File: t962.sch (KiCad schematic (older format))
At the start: 40 parts, among them J1 Conn_01x03, J10 Conn_01x04, J2 TE 282834-8, J3 Conn_01x02_Male, J4 Conn_01x02_Male, J5 Conn_01x02_Male, J7 2.54mm pin header, J8 USB_B_Micro, Q1 BSS214NW, SW1 SW_SPST_KMR2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

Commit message: Added more part number information.
Signed-off-by: Aaron Williams <aaron.w2@gmail.com>
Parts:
- SW2: MFR (none) -> C&K; MPN (none) -> KMR231NG LFS; SPN (none) -> CKN10246CT-ND; SPR (none) -> Digikey; SPURL (none) -> https://www.digikey.com/product-detail/en/c-k/KMR231NG-LFS/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
- U1, U3, U4: MFR (none) -> Maxim; MPN (none) -> MAX31850KATB+; SPN (none) -> MAX31850KATB+-ND; SPR (none) -> Digikey; SPURL (none) -> https://www.digikey.com/product-detail/en/maxim-integrated/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
- U2: MFR (none) -> STMicroelectronics; SPN (none) -> 497-1241-1-ND; SPR (none) -> Digikey; SPURL (none) -> /product-detail/en/stmicroelectronics/LD1117S33CTR/497-1241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
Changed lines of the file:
@@
 F 1 "MAX31850KATB+" H 2250 1934 50  0000 C CNN
 F 2 "Aaron:TDFN-10_3x4mm_P0.5mm" H 2250 1500 50  0001 C CNN
-F 3 "" H 2250 1500 50  0001 C CNN
+F 3 "https://datasheets.maximintegrated.com/en/ds/MAX31850-MAX31851.pdf" H 2250 1500 50  0001 C CNN
+F 4 "Maxim" H 2250 1500 50  0001 C CNN "MFR"
+F 5 "MAX31850KATB+" H 2250 1500 50  0001 C CNN "MPN"
+F 6 "Digikey" H 2250 1500 50  0001 C CNN "SPR"
+F 7 "MAX31850KATB+-ND" H 2250 1500 50  0001 C CNN "SPN"
+F 8 "https://www.digikey.com/product-detail/en/maxim-integrated/MAX31850KATB/MAX31850KATB-ND/3976056" H 2250 1500 50  0001 C CNN "SPURL"
 	1    2250 1500
 	1    0    0    -1
@@
 F 1 "MAX31850KATB+" H 2250 3434 50  0000 C CNN
 F 2 "Aaron:TDFN-10_3x4mm_P0.5mm" H 2250 3000 50  0001 C CNN
-F 3 "" H 2250 3000 50  0001 C CNN
+F 3 "https://datasheets.maximintegrated.com/en/ds/MAX31850-MAX31851.pdf" H 2250 3000 50  0001 C CNN
+F 4 "Maxim" H 2250 3000 50  0001 C CNN "MFR"
+F 5 "MAX31850KATB+" H 2250 3000 50  0001 C CNN "MPN"
+F 6 "Digikey" H 2250 3000 50  0001 C CNN "SPR"
+F 7 "MAX31850KATB+-ND" H 2250 3000 50  0001 C CNN "SPN"
+F 8 "https://www.digikey.com/product-detail/en/maxim-integrated/MAX31850KATB/MAX31850KATB-ND/3976056" H 2250 3000 50  0001 C CNN "SPURL"
 	1    2250 3000
 	1    0    0    -1
@@
 F 1 "MAX31850KATB+" H 2250 4984 50  0000 C CNN
 F 2 "Aaron:TDFN-10_3x4mm_P0.5mm" H 2250 4550 50  0001 C CNN
-F 3 "" H 2250 4550 50  0001 C CNN
+F 3 "https://datasheets.maximintegrated.com/en/ds/MAX31850-MAX31851.pdf" H 2250 4550 50  0001 C CNN
+F 4 "Maxim" H 2250 4550 50  0001 C CNN "MFR"
+F 5 "MAX31850KATB+" H 2250 4550 50  0001 C CNN "MPN"
+F 6 "Digikey" H 2250 4550 50  0001 C CNN "SPR"
+F 7 "MAX31850KATB+-ND" H 2250 4550 50  0001 C CNN "SPN"
+F 8 "https://www.digikey.com/product-detail/en/maxim-integrated/MAX31850KATB/MAX31850KATB-ND/3976056" H 2250 4550 50  0001 C CNN "SPURL"
 	1    2250 4550
 	1    0    0    -1
@@
 F 1 "SW_SPST_KMR2" H 7500 3143 42  0000 C CNN
 F 2 "Aaron:SW_SPST_KMR2" H 7500 2900 50  0001 C CNN
-F 3 "" H 7500 2900 50  0001 C CNN
+F 3 "https://www.ckswitches.com/media/1479/kmr2.pdf" H 7500 2900 50  0001 C CNN
+F 4 "C&K" H 7500 2900 50  0001 C CNN "MFR"
+F 5 "KMR231NG LFS" H 7500 2900 50  0001 C CNN "MPN"
+F 6 "Digikey" H 7500 2900 50  0001 C CNN "SPR"
+F 7 "CKN10246CT-ND" H 7500 2900 50  0001 C CNN "SPN"
+F 8 "https://www.digikey.com/product-detail/en/c-k/KMR231NG-LFS/CKN10246CT-ND/2176497" H 7500 2900 50  0001 C CNN "SPURL"
 	1    7500 2900
 	1    0    0    -1
@@
 F 2 "Package_TO_SOT_SMD:SOT-223" H 4450 2450 60  0001 L CNN
 F 3 "http://www.st.com/content/ccc/resource/technical/document/datasheet/99/3b/7d/91/91/51/4b/be/CD00000544.pdf/files/CD00000544.pdf/jcr:content/translations/en.CD00000544.pdf" H 4450 2550 60  0001 L CNN
-F 4 "497-1241-1-ND" H 4450 2650 60  0001 L CNN "Digi-Key_PN"
+F 4 "STMicroelectronics" H 4250 2250 50  0001 C CNN "MFR"
 F 5 "LD1117S33CTR" H 4450 2750 60  0001 L CNN "MPN"
-F 6 "Integrated Circuits (ICs)" H 4450 2850 60  0001 L CNN "Category"
-F 7 "PMIC - Voltage Regulators - Linear" H 4450 2950 60  0001 L CNN "Family"
-F 8 "http://www.st.com/content/ccc/resource/technical/document/datasheet/99/3b/7d/91/91/51/4b/be/CD00000544.pdf/files/CD00000544.pdf/jcr:content/translations/en.CD00000544.pdf" H 4450 3050 60  0001 L CNN "DK_Datasheet_Link"
-F 9 "/product-detail/en/stmicroelectronics/LD1117S33CTR/497-1241-1-ND/586241" H 4450 3150 60  0001 L CNN "DK_Detail_Page"
-F 10 "IC REG LINEAR 3.3V 800MA SOT223" H 4450 3250 60  0001 L CNN "Description"
-F 11 "STMicroelectronics" H 4450 3350 60  0001 L CNN "Manufacturer"
-F 12 "Active" H 4450 3450 60  0001 L CNN "Status"
+F 6 "Digikey" H 4250 2250 50  0001 C CNN "SPR"
+F 7 "497-1241-1-ND" H 4250 2250 50  0001 C CNN "SPN"
+F 8 "/product-detail/en/stmicroelectronics/LD1117S33CTR/497-1241-1-ND/586241" H 4250 2250 50  0001 C CNN "SPURL"
+F 9 "497-1241-1-ND" H 4450 2650 60  0001 L CNN "Digi-Key_PN"
+F 10 "Integrated Circuits (ICs)" H 4450 2850 60  0001 L CNN "Category"
+F 11 "PMIC - Voltage Regulators - Linear" H 4450 2950 60  0001 L CNN "Family"
+F 12 "http://www.st.com/content/ccc/resource/technical/document/datasheet/99/3b/7d/91/91/51/4b/be/CD00000544.pdf/files/CD00000544.pdf/jcr:content/translations/en.CD00000544.pdf" H 4450 3050 60  0001 L CNN "DK_Datasheet_Link"
+F 13 "/product-detail/en/stmicroelectronics/LD1117S33CTR/497-1241-1-ND/586241" H 4450 3150 60  0001 L CNN "DK_Detail_Page"
+F 14 "IC REG LINEAR 3.3V 800MA SOT223" H 4450 3250 60  0001 L CNN "Description"
+F 15 "STMicroelectronics" H 4450 3350 60  0001 L CNN "Manufacturer"
+F 16 "Active" H 4450 3450 60  0001 L CNN "Status"
 	1    4250 2250
 	1    0    0    -1

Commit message: Fixed 12V connectors and USB to serial
This swaps +12 and GND on the 12V and fan connectors and adds a second
12v connector for bypassing the fan control if desired.  Additionally,
the SI2102N is now powered from the 3.3V supply instead of the USB bus.

Updated to revision 1.1.

Signed-off-by: Aaron Williams <aaron.w2@gmail.com>
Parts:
- removed C6: 4.7uF, Capacitor_SMD:C_0603_1608Metric, symbol Device:C
- removed C7: 0.1uF, Capacitor_SMD:C_0603_1608Metric, symbol Device:C
- added J6: Conn_01x02_Male, Connector_JST:JST_XH_B02B-XH-AM_1x02_P2.50mm_Vertical, symbol Connector:Conn_01x02_Male
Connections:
- wire segments 155 -> 153
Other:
- moved on the sheet: C10, C9, SW1, SW2

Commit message: Updated BOM
Signed-off-by: Aaron Williams <aaron.w2@gmail.com>
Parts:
- C1, C10, C11, C12, C13, C2, C3, C4, C5, C8, C9, H1, H2, H3, H4, J1, J10, J4, J7: MFR (none) -> -; MPN (none) -> -; SPN (none) -> -; SPR (none) -> -; SPURL (none) -> -
- J3, J6: value Conn_01x02_Male -> JST XH-B02B-XH-AM; MFR (none) -> JST; MPN (none) -> B2B-XH-A(LF)(SN); SPN (none) -> 455-2247-ND; SPR (none) -> Digikey; SPURL (none) -> -
- J5: value Conn_01x02_Male -> JST XH-B02B-XH-AM
- R1: MFR (none) -> Yageo; MPN (none) -> RC0603FR-074K7L; SPN (none) -> 311-4.70KHRCT-ND; SPR (none) -> Digikey; SPURL (none) -> -
- R2: MFR (none) -> Yageo; MPN (none) -> AC0603FR-07100KL; SPN (none) -> 311-100KLDCT-ND; SPR (none) -> Digikey; SPURL (none) -> -
- R3: MFR (none) -> Yageo; MPN (none) -> RC0603FR-071KL; SPN (none) -> 311-1.00KHRCT-ND; SPR (none) -> Digikey; SPURL (none) -> -
- R4: MFR (none) -> Panasonic; MPN (none) -> ERJ-3EKF2212V; SPN (none) -> P22.1KHCT-ND; SPR (none) -> Digikey; SPURL (none) -> -
- R5: MFR (none) -> Yageo; MPN (none) -> RC0603FR-0747K5L; SPN (none) -> 311-47.5KHRCT-ND; SPR (none) -> Digikey; SPURL (none) -> -

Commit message: This fixes the VIO input so it is properly powered. Additionally, the footprint for the USBLC6-2SC6 has been fixed to a SOT23-6 which is a bigger footprint than the SOT666 that was there.
Signed-off-by: Aaron Williams <aaron.w2@gmail.com>
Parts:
- D1: footprint Package_TO_SOT_SMD:SOT-666 -> Package_TO_SOT_SMD:SOT-23-6
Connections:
- net labels removed: VIO
- wire segments 153 -> 154

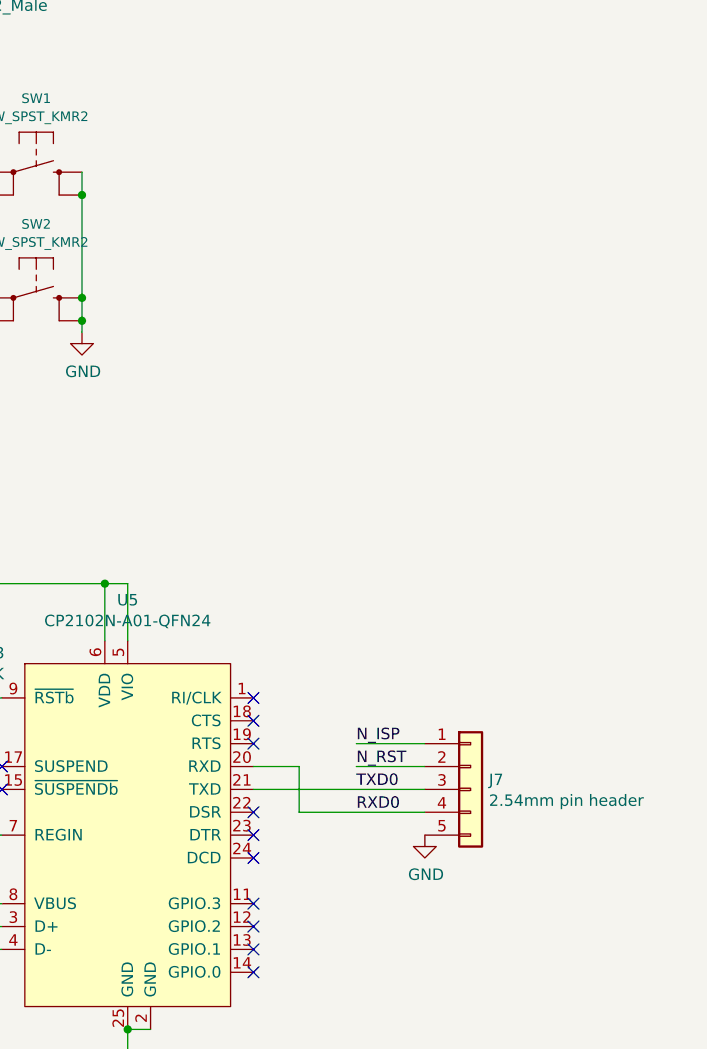
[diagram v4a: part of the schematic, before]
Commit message: Swap TX/RX and add connector to expose RST and NI
TX and RX were swapped from what they should be.  This
fixes that.  Additionally, J9 was added so that external
buttons can be added for NI and RST.

Signed-off-by: aaronw <aaron.w2@gmail.com>
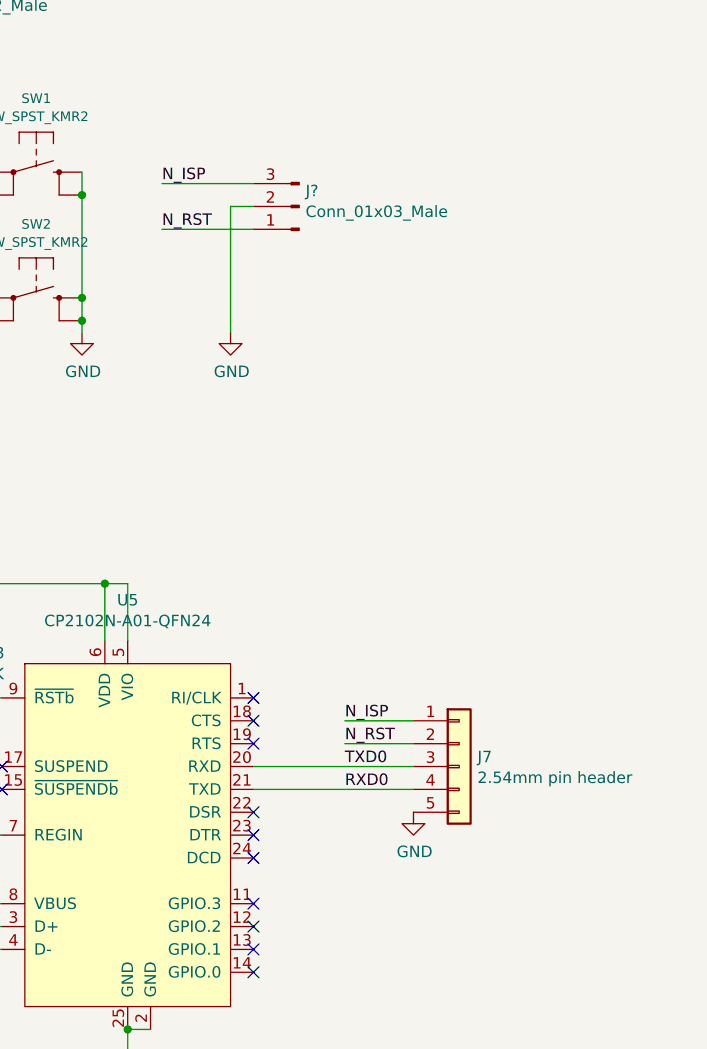
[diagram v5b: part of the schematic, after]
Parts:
- added J?: Conn_01x03_Male, symbol Connector:Conn_01x03_Male
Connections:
- wire segments 154 -> 156
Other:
- moved on the sheet: J7
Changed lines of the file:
@@
 EESchema Schematic File Version 4
 LIBS:t962-cache
-EELAYER 26 0
+EELAYER 29 0
 EELAYER END
 $Descr USLetter 11000 8500
@@
 Sheet 1 1
 Title "T-962 Temperature Monitor Board"
-Date "2019-01-05"
-Rev "1.2"
+Date "2019-03-24"
+Rev "1.2.3"
 Comp ""
 Comment1 "Copyright © 2018 Aaron Williams"
@@
 L Connector_Generic:Conn_01x05 J7
 U 1 1 5BF8D1BE
-P 9400 4800
-F 0 "J7" H 9480 4842 50  0000 L CNN
-F 1 "2.54mm pin header" H 9480 4751 50  0000 L CNN
-F 2 "Connector_PinHeader_2.54mm:PinHeader_1x05_P2.54mm_Vertical" H 9400 4800 50  0001 C CNN
-F 3 "~" H 9400 4800 50  0001 C CNN
-F 4 "-" H 0   0   50  0001 C CNN "MFR"
-F 5 "-" H 0   0   50  0001 C CNN "MPN"
-F 6 "-" H 0   0   50  0001 C CNN "SPR"
-F 7 "-" H 0   0   50  0001 C CNN "SPN"
-F 8 "-" H 0   0   50  0001 C CNN "SPURL"
-	1    9400 4800
+P 9350 4700
+F 0 "J7" H 9430 4742 50  0000 L CNN
+F 1 "2.54mm pin header" H 9430 4651 50  0000 L CNN
+F 2 "Connector_PinHeader_2.54mm:PinHeader_1x05_P2.54mm_Vertical" H 9350 4700 50  0001 C CNN
+F 3 "~" H 9350 4700 50  0001 C CNN
+F 4 "-" H -50 -100 50  0001 C CNN "MFR"
+F 5 "-" H -50 -100 50  0001 C CNN "MPN"
+F 6 "-" H -50 -100 50  0001 C CNN "SPR"
+F 7 "-" H -50 -100 50  0001 C CNN "SPN"
+F 8 "-" H -50 -100 50  0001 C CNN "SPURL"
+	1    9350 4700
 	1    0    0    -1
 $EndComp
@@
 L power:GND #PWR030
 U 1 1 5BF90085
-P 9200 5000
-F 0 "#PWR030" H 9200 4750 50  0001 C CNN
-F 1 "GND" H 9205 4827 50  0000 C CNN
-F 2 "" H 9200 5000 50  0001 C CNN
-F 3 "" H 9200 5000 50  0001 C CNN
-	1    9200 5000
+P 9150 4900
+F 0 "#PWR030" H 9150 4650 50  0001 C CNN
+F 1 "GND" H 9155 4727 50  0000 C CNN
+F 2 "" H 9150 4900 50  0001 C CNN
+F 3 "" H 9150 4900 50  0001 C CNN
+	1    9150 4900
 	1    0    0    -1
 $EndComp
@@
 Text Label 3500 1150 0    50   ~ 0
 FAN_PWM
-Text Label 8900 4600 0    50   ~ 0
+Text Label 8850 4500 0    50   ~ 0
 N_ISP
-Text Label 8900 4700 0    50   ~ 0
+Text Label 8850 4600 0    50   ~ 0
 N_RST
-Text Label 8900 4800 0    50   ~ 0
+Text Label 8850 4700 0    50   ~ 0
 TXD0
-Text Label 8900 4900 0    50   ~ 0
+Text Label 8850 4800 0    50   ~ 0
 RXD0
 Text Label 7000 2100 0    50   ~ 0
@@
 	5650 3900 7000 3900
 Wire Wire Line
-	9200 4600 8900 4600
-Wire Wire Line
-	8900 4700 9200 4700
-Wire Wire Line
-	8450 4800 9200 4800
-Wire Wire Line
-	8450 4700 8650 4700
-Wire Wire Line
-	8650 4700 8650 4900
-Wire Wire Line
-	8650 4900 9200 4900
+	9150 4500 8850 4500
+Wire Wire Line
+	8850 4600 9150 4600
 Wire Wire Line
 	7900 5950 7900 5850
@@
 Wire Wire Line
 	7800 3900 7800 4150
+Wire Wire Line
+	7200 3900 7800 3900
+Wire Wire Line
+	7200 3900 7200 4100
+Wire Wire Line
+	7900 3900 7800 3900
+Wire Wire Line
+	7900 3900 7900 4150
 Connection ~ 1800 950
 Connection ~ 1700 1800
@@
 Connection ~ 4900 2250
 Connection ~ 7000 3900
+Connection ~ 7200 3900
+Connection ~ 7800 3900
 NoConn ~ 7350 4700
 NoConn ~ 7350 4800
@@
 NoConn ~ 8450 5600
 NoConn ~ 5150 5300
-Connection ~ 7200 3900
-Wire Wire Line
-	7200 3900 7800 3900
-Wire Wire Line
-	7200 3900 7200 4100
-Wire Wire Line
-	7900 3900 7800 3900
-Wire Wire Line
-	7900 3900 7900 4150
-Connection ~ 7800 3900
+Wire Wire Line
+	8450 4800 9150 4800
+Wire Wire Line
+	8450 4700 9150 4700
+Text Label 8050 2150 0    50   ~ 0
+N_ISP
+Text Label 8050 2350 0    50   ~ 0
+N_RST
+$Comp
+L power:GND #PWR022
+U 1 1 5C9D63D4
+P 8350 2800
+F 0 "#PWR022" H 8350 2550 50  0001 C CNN
+F 1 "GND" H 8355 2627 50  0000 C CNN
+F 2 "" H 8350 2800 50  0001 C CNN
+F 3 "" H 8350 2800 50  0001 C CNN
+	1    8350 2800
+	1    0    0    -1
+$EndComp
+Wire Wire Line
+	8050 2350 8450 2350
+Wire Wire Line
+	8050 2150 8450 2150
+Wire Wire Line
+	8450 2250 8350 2250
+$Comp
+L Connector:Conn_01x03_Male J?
+U 1 1 5CA04CCC
+P 8650 2250
+F 0 "J?" H 8622 2182 50  0000 R CNN
+F 1 "Conn_01x03_Male" H 8622 2273 50  0000 R CNN
+F 2 "" H 8650 2250 50  0001 C CNN
+F 3 "~" H 8650 2250 50  0001 C CNN
+	1    8650 2250
+	-1   0    0    1
+$EndComp
+Wire Wire Line
+	8350 2250 8350 2800
 $EndSCHEMATC
